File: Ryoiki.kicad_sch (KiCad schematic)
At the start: 45 parts, among them J1 USB_C_Receptacle, J2 Conn_02x06, SW1 bootsel, SW2 restart, U1 W25Q32JVSS, U2 TLV74333PDBVR, U3 RP2040, Y1 12Mhz

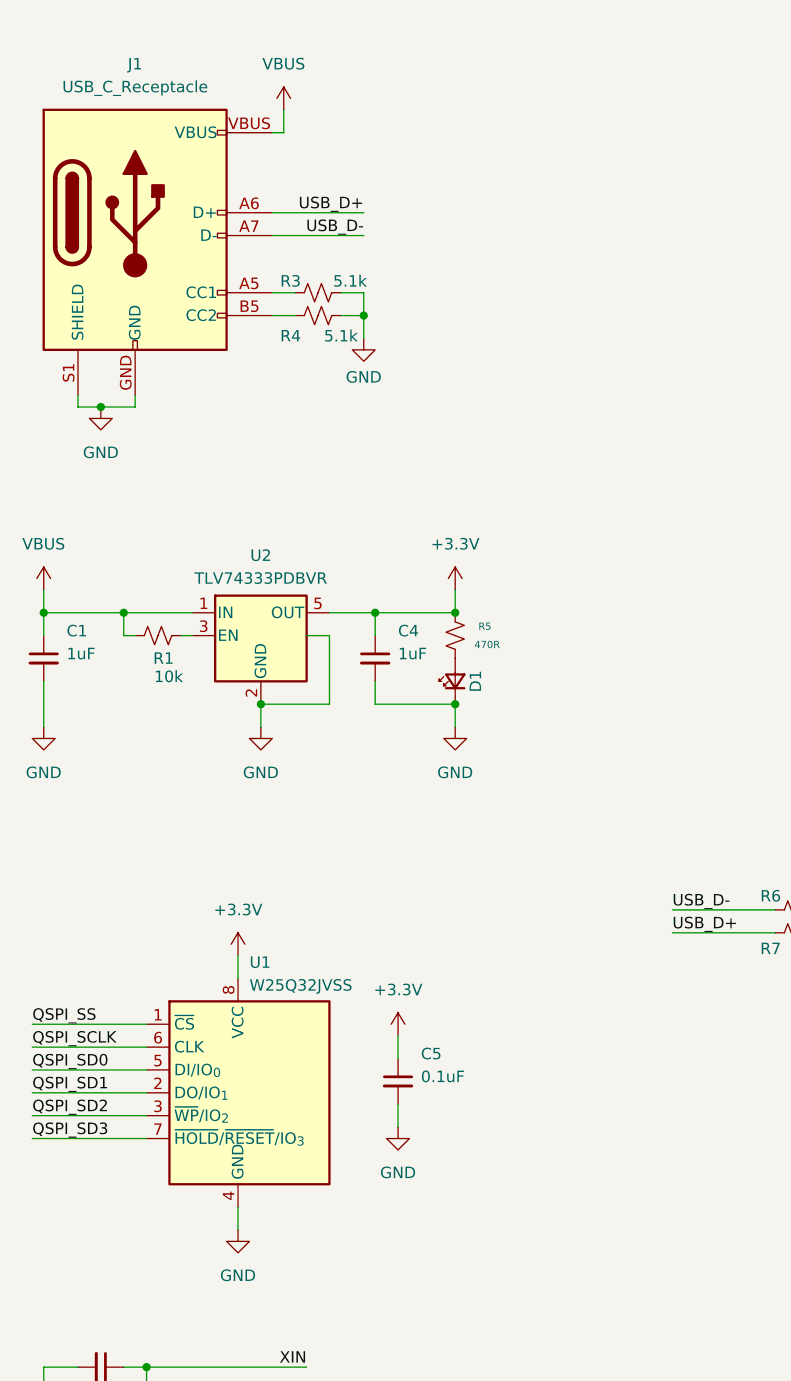
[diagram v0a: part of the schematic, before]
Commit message: - Added ESD protection (USBLC6-2SC6) to the USB data lines and VBUS. - add more satoru gojo
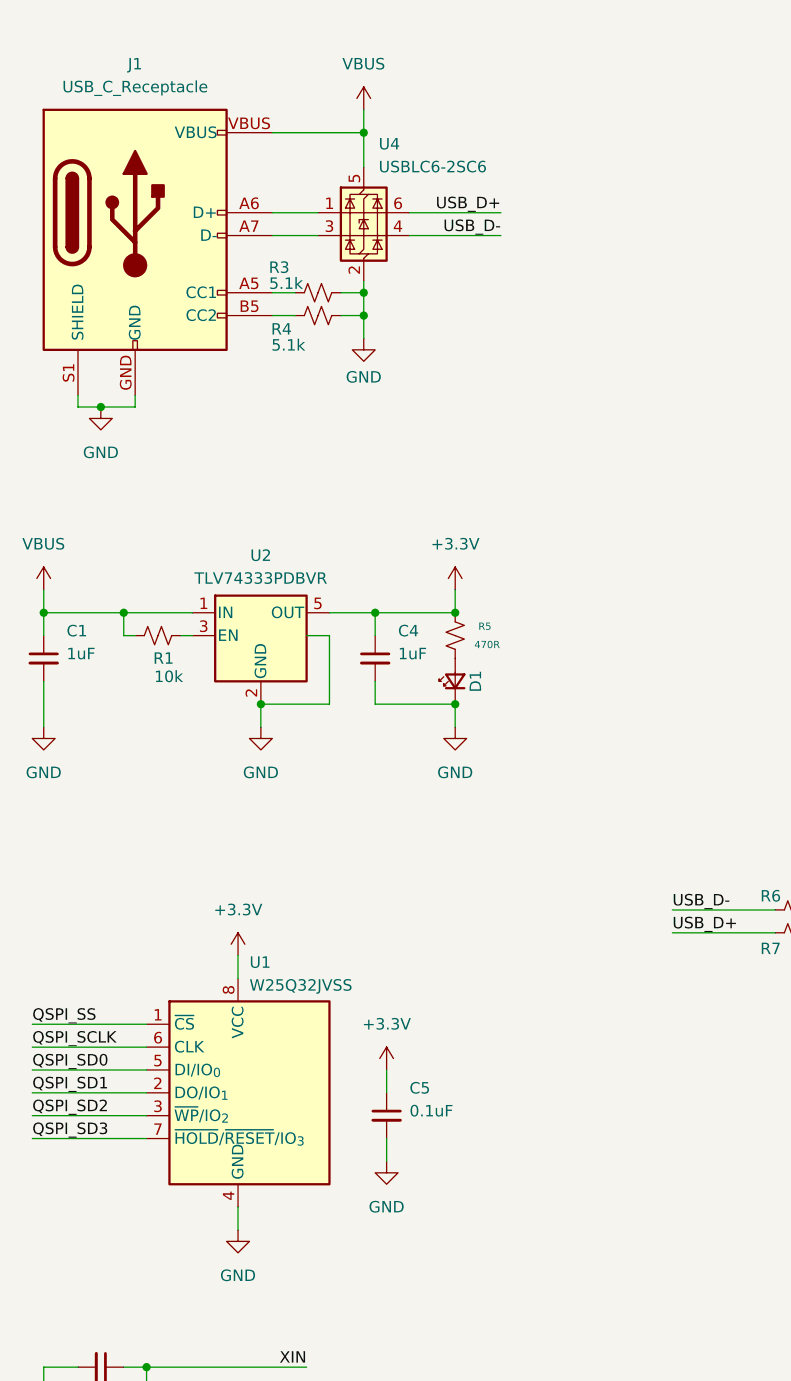
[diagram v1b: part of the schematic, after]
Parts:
- added U4: USBLC6-2SC6, Package_TO_SOT_SMD:SOT-23-6, symbol Power_Protection:USBLC6-2SC6
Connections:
- net GND: now also U4.2 (GND)
- net USB_D+: now also U4.6 (I/O1); no longer J1.A6 (D+), J1.B6 (D+)
- net USB_D-: now also U4.4 (I/O2); no longer J1.A7 (D-), J1.B7 (D-)
- net VBUS: now also U4.5 (VBUS)
- new net: J1.A6 (D+), J1.B6 (D+), U4.1 (I/O1)
- new net: J1.A7 (D-), J1.B7 (D-), U4.3 (I/O2)
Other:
- moved on the sheet: C5
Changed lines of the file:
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@@
 	)
 	(junction
+		(at 54.61 45.72)
+		(diameter 0)
+		(color 0 0 0 0)
+	)
+	(junction
 		(at 161.29 60.96)
 		(diameter 0)
@@
 	)
 	(junction
+		(at 54.61 27.94)
+		(diameter 0)
+		(color 0 0 0 0)
+	)
+	(junction
 		(at 19.05 81.28)
 		(diameter 0)
@@
 	(wire
 		(pts
-			(xy 44.45 36.83) (xy 54.61 36.83)
+			(xy 59.69 36.83) (xy 69.85 36.83)
 		)
 		(stroke
@@
 	(wire
 		(pts
-			(xy 45.72 27.94) (xy 45.72 25.4)
+			(xy 54.61 27.94) (xy 54.61 25.4)
 		)
 		(stroke
@@
 	(wire
 		(pts
-			(xy 58.42 135.89) (xy 58.42 138.43)
+			(xy 57.15 139.7) (xy 57.15 142.24)
 		)
 		(stroke
@@
 	(wire
 		(pts
+			(xy 44.45 39.37) (xy 49.53 39.37)
+		)
+		(stroke
+			(width 0)
+			(type default)
+		)
+	)
+	(wire
+		(pts
 			(xy 137.16 50.8) (xy 137.16 53.34)
 		)
@@
 	(wire
 		(pts
-			(xy 44.45 27.94) (xy 45.72 27.94)
+			(xy 44.45 27.94) (xy 54.61 27.94)
 		)
 		(stroke
@@
 	(wire
 		(pts
+			(xy 54.61 31.75) (xy 54.61 27.94)
+		)
+		(stroke
+			(width 0)
+			(type default)
+		)
+	)
+	(wire
+		(pts
 			(xy 55.88 81.28) (xy 55.88 83.82)
 		)
@@
 	(wire
 		(pts
+			(xy 54.61 44.45) (xy 54.61 45.72)
+		)
+		(stroke
+			(width 0)
+			(type default)
+		)
+	)
+	(wire
+		(pts
 			(xy 137.16 60.96) (xy 125.73 60.96)
 		)
@@
 	(wire
 		(pts
+			(xy 44.45 36.83) (xy 49.53 36.83)
+		)
+		(stroke
+			(width 0)
+			(type default)
+		)
+	)
+	(wire
+		(pts
 			(xy 125.73 58.42) (xy 125.73 60.96)
 		)
@@
 	(wire
 		(pts
-			(xy 58.42 128.27) (xy 58.42 130.81)
+			(xy 57.15 132.08) (xy 57.15 134.62)
 		)
 		(stroke
@@
 	(wire
 		(pts
-			(xy 44.45 39.37) (xy 54.61 39.37)
+			(xy 59.69 39.37) (xy 69.85 39.37)
 		)
 		(stroke
@@
 	)
 	(label "USB_D+"
-		(at 54.61 36.83 180)
+		(at 69.85 36.83 180)
 		(effects
 			(font
@@
 	)
 	(label "USB_D-"
-		(at 54.61 39.37 180)
+		(at 69.85 39.37 180)
 		(effects
 			(font
@@
 		(dnp no)
 		(property "Reference" "R3"
-			(at 46.482 44.45 0)
+			(at 45.212 42.926 0)
 			(effects
 				(font
@@
 		)
 		(property "Value" "5.1k"
-			(at 53.086 44.45 0)
+			(at 45.974 44.704 0)
 			(effects
 				(font
@@
 	(symbol
 		(lib_id "power:+3.3V")
-		(at 58.42 128.27 0)
+		(at 57.15 132.08 0)
 		(unit 1)
 		(exclude_from_sim no)
@@
 		(fields_autoplaced yes)
 		(property "Reference" "#PWR010"
-			(at 58.42 132.08 0)
+			(at 57.15 135.89 0)
 			(effects
 				(font
@@
 		)
 		(property "Value" "+3.3V"
-			(at 58.42 123.19 0)
+			(at 57.15 127 0)
 			(effects
 				(font
@@
 		)
 		(property "Footprint" ""
-			(at 58.42 128.27 0)
+			(at 57.15 132.08 0)
 			(effects
 				(font
@@
 		)
 		(property "Datasheet" ""
-			(at 58.42 128.27 0)
+			(at 57.15 132.08 0)
 			(effects
 				(font
@@
 		)
 		(property "Description" "Power symbol creates a global label with name \"+3.3V\""
-			(at 58.42 128.27 0)
+			(at 57.15 132.08 0)
 			(effects
 				(font
@@
 	(symbol
 		(lib_id "power:GND")
-		(at 58.42 138.43 0)
+		(at 57.15 142.24 0)
 		(unit 1)
 		(exclude_from_sim no)
@@
 		(fields_autoplaced yes)
 		(property "Reference" "#PWR011"
-			(at 58.42 144.78 0)
+			(at 57.15 148.59 0)
 			(effects
 				(font
@@
 		)
 		(property "Value" "GND"
-			(at 58.42 143.51 0)
+			(at 57.15 147.32 0)
 			(effects
 				(font
@@
 		)
 		(property "Footprint" ""
-			(at 58.42 138.43 0)
+			(at 57.15 142.24 0)
 			(effects
 				(font
@@
 		)
 		(property "Datasheet" ""
-			(at 58.42 138.43 0)
+			(at 57.15 142.24 0)
 			(effects
 				(font
@@
 		)
 		(property "Description" "Power symbol creates a global label with name \"GND\" , ground"
-			(at 58.42 138.43 0)
+			(at 57.15 142.24 0)
 			(effects
 				(font
@@
 	)
 	(symbol
+		(lib_id "Power_Protection:USBLC6-2SC6")
+		(at 54.61 36.83 0)
+		(unit 1)
+		(exclude_from_sim no)
+		(in_bom yes)
+		(on_board yes)
+		(dnp no)
+		(property "Reference" "U4"
+			(at 56.2611 29.21 0)
+			(effects
+				(font
+					(size 1.27 1.27)
+				)
+				(justify left)
+			)
+		)
+		(property "Value" "USBLC6-2SC6"
+			(at 56.2611 31.75 0)
+			(effects
+				(font
+					(size 1.27 1.27)
+				)
+				(justify left)
+			)
+		)
+		(property "Footprint" "Package_TO_SOT_SMD:SOT-23-6"
+			(at 55.88 43.18 0)
+			(effects
+				(font
+					(size 1.27 1.27)
+					(italic yes)
+				)
+				(justify left)
+				(hide yes)
+			)
+		)
+		(property "Datasheet" "https://www.st.com/resource/en/datasheet/usblc6-2.pdf"
+			(at 55.88 45.085 0)
+			(effects
+				(font
+					(size 1.27 1.27)
+				)
+				(justify left)
+				(hide yes)
+			)
+		)
+		(property "Description" "Very low capacitance ESD protection diode, 2 data-line, SOT-23-6"
+			(at 54.61 36.83 0)
+			(effects
+				(font
+					(size 1.27 1.27)
+				)
+				(hide yes)
+			)
+		)
+		(pin "6"
+		)
+		(pin "2"
+		)
+		(pin "5"
+		)
+		(pin "3"
+		)
+		(pin "1"
+		)
+		(pin "4"
+		)
+		(instances
+			(project ""
+				(path "/657fcd3c-5524-4427-aec8-0169a5808275"
+					(reference "U4")
+					(unit 1)
+				)
+			)
+		)
+	)
+	(symbol
 		(lib_id "power:+3.3V")
 		(at 64.77 78.74 0)
@@
 	(symbol
 		(lib_id "power:VBUS")
-		(at 45.72 25.4 0)
+		(at 54.61 25.4 0)
 		(unit 1)
 		(exclude_from_sim no)
@@
 		(fields_autoplaced yes)
 		(property "Reference" "#PWR08"
-			(at 45.72 29.21 0)
+			(at 54.61 29.21 0)
 			(effects
 				(font
@@
 		)
 		(property "Value" "VBUS"
-			(at 45.72 20.32 0)
+			(at 54.61 20.32 0)
 			(effects
 				(font
@@
 		)
 		(property "Footprint" ""
-			(at 45.72 25.4 0)
+			(at 54.61 25.4 0)
 			(effects
 				(font
@@
 		)
 		(property "Datasheet" ""
-			(at 45.72 25.4 0)
+			(at 54.61 25.4 0)
 			(effects
 				(font
@@
 		)
 		(property "Description" "Power symbol creates a global label with name \"VBUS\""
-			(at 45.72 25.4 0)
+			(at 54.61 25.4 0)
 			(effects
 				(font
@@
 		(dnp no)
 		(property "Reference" "R4"
-			(at 46.482 50.546 0)
+			(at 45.466 49.784 0)
 			(effects
 				(font
@@
 		)
 		(property "Value" "5.1k"
-			(at 52.07 50.546 0)
+			(at 46.228 51.562 0)
 			(effects
 				(font
@@
 	(symbol
 		(lib_id "PCM_SparkFun-Capacitor:0.1uF_0603_25V_20%")
-		(at 58.42 133.35 0)
+		(at 57.15 137.16 0)
 		(unit 1)
 		(exclude_from_sim no)
@@
 		(dnp no)
 		(property "Reference" "C5"
-			(at 60.96 130.302 0)
+			(at 59.69 134.112 0)
 			(effects
 				(font
@@
 		)
 		(property "Value" "0.1uF"
-			(at 60.96 132.842 0)
+			(at 59.69 136.652 0)
 			(effects
 				(font
@@
 		)
 		(property "Footprint" "Capacitor_SMD:C_0402_1005Metric_Pad0.74x0.62mm_HandSolder"
-			(at 58.42 144.78 0)
+			(at 57.15 148.59 0)
 			(effects
 				(font
@@
 		)
 		(property "Datasheet" ""
-			(at 58.42 147.32 0)
+			(at 57.15 151.13 0)
 			(effects
 				(font
@@
 		)
 		(property "Description" ""
-			(at 65.278 137.414 0)
+			(at 64.008 141.224 0)
 			(effects
 				(font
@@
 		)
 		(property "PROD_ID" "CAP-00810"
-			(at 58.42 149.86 0)
+			(at 57.15 153.67 0)
 			(effects
 				(font
@@
 		)
 		(property "Voltage" "25V"
-			(at 60.96 135.382 0)
+			(at 59.69 139.192 0)
 			(effects
 				(font
@@
 		)
 		(property "Tolerance" ""
-			(at 60.96 137.1662 0)
+			(at 59.69 140.9762 0)
 			(effects
 				(font
